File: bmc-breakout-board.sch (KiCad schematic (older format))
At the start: 42 parts, among them J1 PinHeader_2x4, J10 PinHeader_2x4, J11 PinHeader_2x05, J12 61300411121, J14 PCIE_BUS_x1, J15 0473460001, J16 PinHeader_1x07, J17 UE27AC54100, J2 PinHeader_2x13, J3 PinHeader_2x08, J4 61300411121, J5 ME1016813401101, J6 61300411121, J7 DC_SOCKET, J8 PinHeader_2x05, J9 PinHeader_1x07, Q1 BSS138AKA

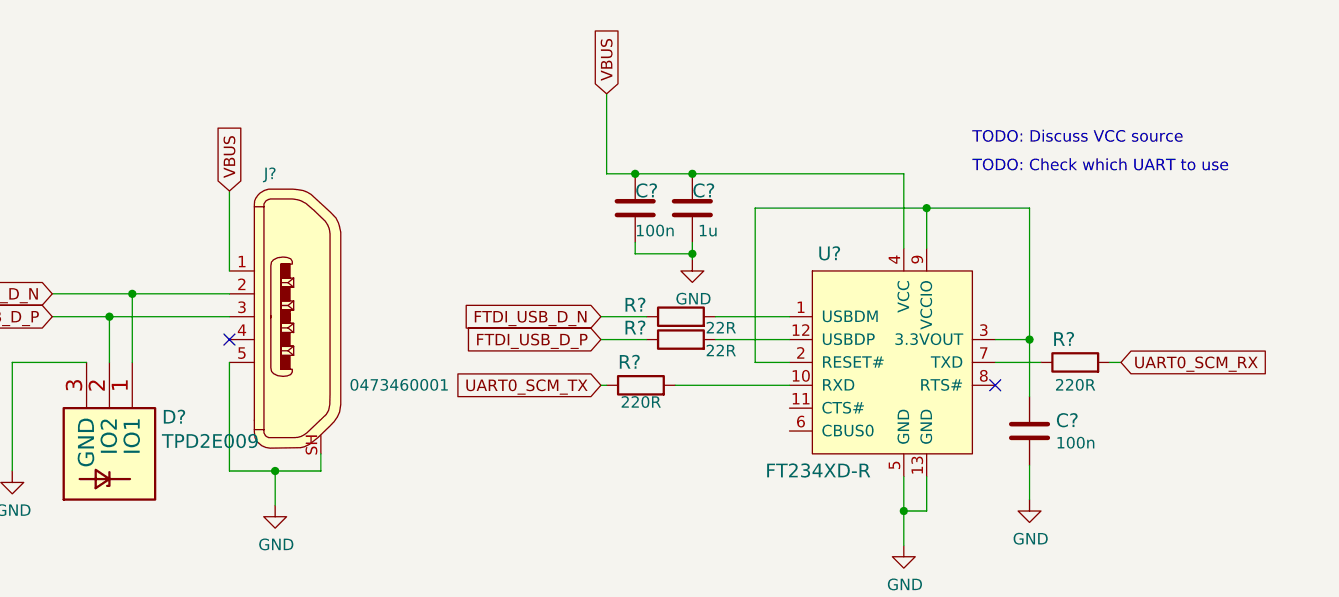
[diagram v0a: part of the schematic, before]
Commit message: Add FTDI circuit on PCB and do routing
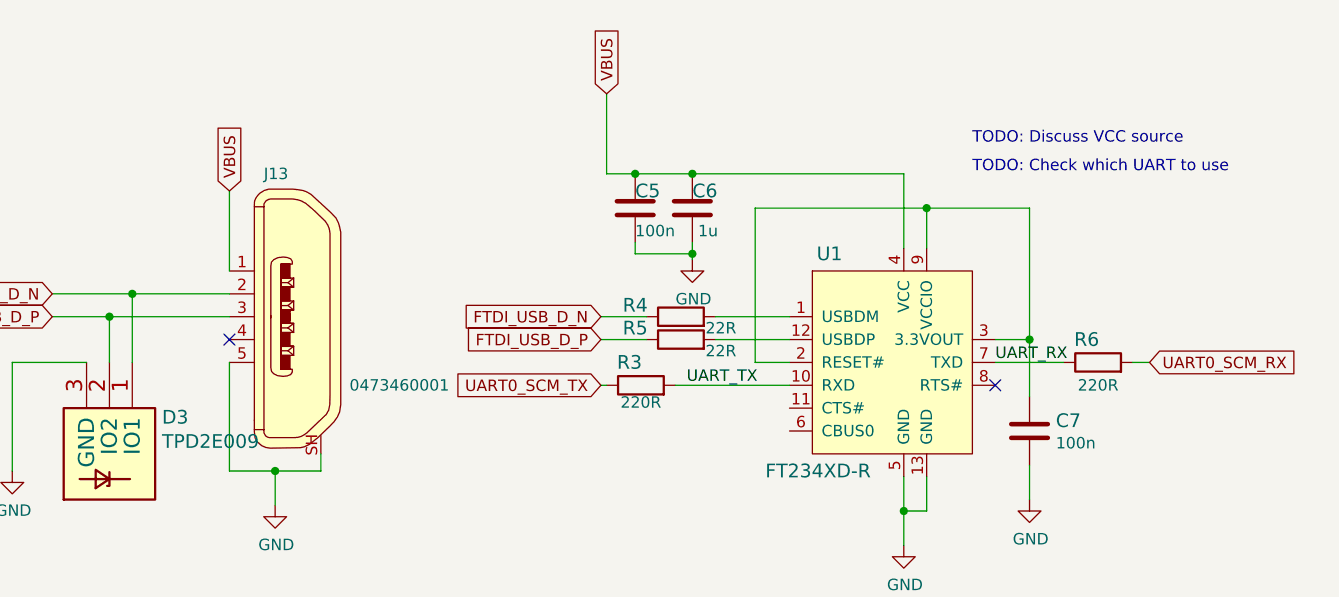
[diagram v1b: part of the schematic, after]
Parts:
- gave numbers to parts that had none: 10
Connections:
- net labels added: UART_RX, UART_TX
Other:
- moved on the sheet: R6
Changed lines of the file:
@@
 GND probes
 $Comp
-L bmc-breakout-board:FT234XD-R U?
+L bmc-breakout-board:FT234XD-R U1
 U 1 1 619D808C
 P 14225 6100
-F 0 "U?" H 14000 6475 60  0000 C CNN
+F 0 "U1" H 14000 6475 60  0000 C CNN
 F 1 "FT234XD-R" H 13950 5525 60  0000 C CNN
 F 2 "bmc-breakout-board-footprints:DFN-12-1EP_3x3mm" H 14425 6300 60  0001 L CNN
@@
 Connection ~ 14325 6850
 $Comp
-L bmc-breakout-board:GND #PWR?
+L bmc-breakout-board:GND #PWR0113
 U 1 1 61AF1FE7
 P 14325 7000
-F 0 "#PWR?" H 14325 6750 50  0001 C CNN
+F 0 "#PWR0113" H 14325 6750 50  0001 C CNN
 F 1 "GND" H 14330 6827 50  0000 C CNN
 F 2 "" H 14325 7000 50  0001 C CNN
@@
 	13000 6300 13025 6300
 Wire Wire Line
-	14725 6200 14925 6200
+	14725 6200 15025 6200
 Text GLabel 13000 6300 0    50   Input ~ 0
 UART0_SCM_TX
-Text GLabel 15275 6200 2    50   Input ~ 0
+Text GLabel 15400 6200 2    50   Input ~ 0
 UART0_SCM_RX
 $Comp
-L bmc-breakout-board:R_220R_0402 R?
+L bmc-breakout-board:R_220R_0402 R6
 U 1 1 61BE88F3
-P 15075 6200
-F 0 "R?" H 15025 6300 60  0000 C CNN
-F 1 "R_220R_0402" H 15075 6050 60  0001 C CNN
-F 2 "bmc-breakout-board-footprints:0402-res" H 15275 6400 60  0001 L CNN
-F 3 "" H 15075 6200 50  0001 C CNN
-F 4 "Panasonic" H 15275 6600 60  0001 L CNN "Manufacturer"
-F 5 "ERJ2GEJ221X" H 15275 6500 60  0001 L CNN "MPN"
-F 6 "220R" H 15075 6100 50  0000 C CNN "Val"
-	1    15075 6200
-	1    0    0    -1
-$EndComp
-$Comp
-L bmc-breakout-board:R_220R_0402 R?
+P 15175 6200
+F 0 "R6" H 15125 6300 60  0000 C CNN
+F 1 "R_220R_0402" H 15175 6050 60  0001 C CNN
+F 2 "bmc-breakout-board-footprints:0402-res" H 15375 6400 60  0001 L CNN
+F 3 "" H 15175 6200 50  0001 C CNN
+F 4 "Panasonic" H 15375 6600 60  0001 L CNN "Manufacturer"
+F 5 "ERJ2GEJ221X" H 15375 6500 60  0001 L CNN "MPN"
+F 6 "220R" H 15175 6100 50  0000 C CNN "Val"
+	1    15175 6200
+	1    0    0    -1
+$EndComp
+$Comp
+L bmc-breakout-board:R_220R_0402 R3
 U 1 1 61BE8BB6
 P 13175 6300
-F 0 "R?" H 13125 6400 60  0000 C CNN
+F 0 "R3" H 13125 6400 60  0000 C CNN
 F 1 "R_220R_0402" H 13175 6150 60  0001 C CNN
 F 2 "bmc-breakout-board-footprints:0402-res" H 13375 6500 60  0001 L CNN
@@
 	13325 6300 13825 6300
 Wire Wire Line
-	15225 6200 15275 6200
-$Comp
-L bmc-breakout-board:C_100n_0402 C?
+	15325 6200 15400 6200
+$Comp
+L bmc-breakout-board:C_100n_0402 C7
 U 1 1 61C08691
 P 14875 6500
-F 0 "C?" H 14760 6455 60  0000 R CNN
+F 0 "C7" H 14760 6455 60  0000 R CNN
 F 1 "C_100n_0402" H 14875 6350 60  0001 C CNN
 F 2 "bmc-breakout-board-footprints:0402-cap" H 15075 6700 60  0001 L CNN
@@
 	14875 6650 14875 6800
 $Comp
-L bmc-breakout-board:GND #PWR?
+L bmc-breakout-board:GND #PWR0114
 U 1 1 61C4C68C
 P 14875 6800
-F 0 "#PWR?" H 14875 6550 50  0001 C CNN
+F 0 "#PWR0114" H 14875 6550 50  0001 C CNN
 F 1 "GND" H 14880 6627 50  0000 C CNN
 F 2 "" H 14875 6800 50  0001 C CNN
@@
 	13025 5375 13150 5375
 $Comp
-L bmc-breakout-board:C_100n_0402 C?
+L bmc-breakout-board:C_100n_0402 C5
 U 1 1 61D03EE4
 P 13150 5525
-F 0 "C?" H 13150 5450 60  0000 R CNN
+F 0 "C5" H 13150 5450 60  0000 R CNN
 F 1 "C_100n_0402" H 13150 5375 60  0001 C CNN
 F 2 "bmc-breakout-board-footprints:0402-cap" H 13350 5725 60  0001 L CNN
@@
 	13150 5375 13400 5375
 $Comp
-L bmc-breakout-board:C_1u_0402 C?
+L bmc-breakout-board:C_1u_0402 C6
 U 1 1 61D40FF8
 P 13400 5525
-F 0 "C?" H 13400 5600 60  0000 L CNN
+F 0 "C6" H 13400 5600 60  0000 L CNN
 F 1 "C_1u_0402" H 13400 5375 60  0001 C CNN
 F 2 "bmc-breakout-board-footprints:0402-cap" H 13600 5725 60  0001 L CNN
@@
 Connection ~ 13400 5725
 $Comp
-L bmc-breakout-board:GND #PWR?
+L bmc-breakout-board:GND #PWR0115
 U 1 1 61D45FD6
 P 13400 5750
-F 0 "#PWR?" H 13400 5500 50  0001 C CNN
+F 0 "#PWR0115" H 13400 5500 50  0001 C CNN
 F 1 "GND" H 13405 5577 50  0000 C CNN
 F 2 "" H 13400 5750 50  0001 C CNN
@@
 $EndComp
 $Comp
-L bmc-breakout-board:R_22R_0402 R?
+L bmc-breakout-board:R_22R_0402 R5
 U 1 1 61DDB24D
 P 13350 6100
-F 0 "R?" H 13150 6150 60  0000 C CNN
+F 0 "R5" H 13150 6150 60  0000 C CNN
 F 1 "R_22R_0402" H 13350 5950 60  0001 C CNN
 F 2 "bmc-breakout-board-footprints:0402-res" H 13550 6300 60  0001 L CNN
@@
 $EndComp
 $Comp
-L bmc-breakout-board:R_22R_0402 R?
+L bmc-breakout-board:R_22R_0402 R4
 U 1 1 61E3AA54
 P 13350 6000
-F 0 "R?" H 13150 6050 60  0000 C CNN
+F 0 "R4" H 13150 6050 60  0000 C CNN
 F 1 "R_22R_0402" H 13350 5850 60  0001 C CNN
 F 2 "bmc-breakout-board-footprints:0402-res" H 13550 6200 60  0001 L CNN
@@
 VBUS
 $Comp
-L bmc-breakout-board:TPD2E009 D?
+L bmc-breakout-board:TPD2E009 D3
 U 1 1 61F54A7F
 P 10950 6400
-F 0 "D?" V 10990 6530 60  0000 L CNN
+F 0 "D3" V 10990 6530 60  0000 L CNN
 F 1 "TPD2E009" V 11096 6530 60  0000 L CNN
 F 2 "bmc-breakout-board-footprints:SOT-3" H 11000 6600 60  0001 C CNN
@@
 	10425 6200 10425 6675
 $Comp
-L bmc-breakout-board:GND #PWR?
+L bmc-breakout-board:GND #PWR0116
 U 1 1 61F54A8D
 P 10425 6675
-F 0 "#PWR?" H 10425 6425 50  0001 C CNN
+F 0 "#PWR0116" H 10425 6425 50  0001 C CNN
 F 1 "GND" H 10430 6502 50  0000 C CNN
 F 2 "" H 10425 6675 50  0001 C CNN
@@
 	11375 6675 11575 6675
 $Comp
-L bmc-breakout-board:GND #PWR?
+L bmc-breakout-board:GND #PWR0117
 U 1 1 61F54A94
 P 11575 6825
-F 0 "#PWR?" H 11575 6575 50  0001 C CNN
+F 0 "#PWR0117" H 11575 6575 50  0001 C CNN
 F 1 "GND" H 11580 6652 50  0000 C CNN
 F 2 "" H 11575 6825 50  0001 C CNN
@@
 NoConn ~ 11375 6100
 $Comp
-L bmc-breakout-board:0473460001 J?
+L bmc-breakout-board:0473460001 J13
 U 1 1 61F54AA2
 P 11675 6000
-F 0 "J?" H 11825 6625 50  0000 R CNN
+F 0 "J13" H 11825 6625 50  0000 R CNN
 F 1 "0473460001" H 11450 5700 50  0000 R CNN
 F 2 "bmc-breakout-board-footprints:USB_Micro_B_Female_0473460001" H 11875 6200 60  0001 L CNN
@@
 Text GLabel 10600 5900 0    50   Input ~ 0
 FTDI_USB_D_N
+Text Label 13375 6300 0    50   ~ 0
+UART_TX
+Text Label 14725 6200 0    50   ~ 0
+UART_RX
 $EndSCHEMATC

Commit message: Add power filtering
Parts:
- added C? (x2): C_100n_0402_16V, antmicro-footprints:0402-cap, symbol antmicroCapacitorsmisc:C_100n_0402_16V
- added C?: C_3u3_1206_100V, antmicro-footprints:1206-cap, symbol antmicroCapacitorsmisc:C_3u3_1206_100V
- added L?: 744235900, antmicro-footprints:744235900, symbol antmicroFixedInductors:744235900
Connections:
- net labels added: P12V_AUX_IN
- wire segments 340 -> 359
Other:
- note added: "Power filtering"
- moved on the sheet: J14, R1, R2

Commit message: Update filtering circuit
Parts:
- removed C?: C_3u3_1206_100V, antmicro-footprints:1206-cap, symbol antmicroCapacitorsmisc:C_3u3_1206_100V
- added C?: C_10u_25V_0603, bmc-breakout-board-footprints:0603-cap, symbol bmc-breakout-board:C_10u_25V_0603
- added C? (x2): C_1n_0603, bmc-breakout-board-footprints:0603-cap, symbol bmc-breakout-board:C_1n_0603
- C? (x2): footprint antmicro-footprints:0402-cap -> bmc-breakout-board-footprints:0402-cap; symbol antmicroCapacitorsmisc:C_100n_0402_16V -> bmc-breakout-board:C_100n_0402_16V
- L?: footprint antmicro-footprints:744235900 -> bmc-breakout-board-footprints:744235900; symbol antmicroFixedInductors:744235900 -> bmc-breakout-board:744235900
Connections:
- net labels added: GND_IN
- wire segments 359 -> 368
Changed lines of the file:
@@
 Wire Wire Line
 	14450 3125 14450 3525
-$Comp
-L bmc-breakout-board:GND #PWR0110
-U 1 1 60D4DCD1
-P 14450 3675
-F 0 "#PWR0110" H 14450 3425 50  0001 C CNN
-F 1 "GND" H 14455 3502 50  0000 C CNN
-F 2 "" H 14450 3675 50  0001 C CNN
-F 3 "" H 14450 3675 50  0001 C CNN
-	1    14450 3675
-	1    0    0    -1
-$EndComp
 Wire Wire Line
 	14450 3125 14575 3125
@@
 	14450 3525 14575 3525
 Connection ~ 14450 3525
-Wire Wire Line
-	14450 3525 14450 3675
 Wire Wire Line
 	14575 3325 14325 3325
@@
 UART_RX
 $Comp
-L antmicroCapacitorsmisc:C_100n_0402_16V C?
+L bmc-breakout-board:C_100n_0402_16V C?
 U 1 1 6211016B
 P 13450 4300
 F 0 "C?" H 13565 4345 60  0000 L CNN
 F 1 "C_100n_0402_16V" H 13450 4150 60  0001 C CNN
-F 2 "antmicro-footprints:0402-cap" H 13650 4500 60  0001 L CNN
+F 2 "bmc-breakout-board-footprints:0402-cap" H 13650 4500 60  0001 L CNN
 F 3 "" H 13450 4300 50  0001 C CNN
 F 4 "MULTICOMP" H 13650 4700 60  0001 L CNN "Manufacturer"
@@
 $EndComp
 $Comp
-L antmicroCapacitorsmisc:C_3u3_1206_100V C?
-U 1 1 62116EE7
-P 14925 4300
-F 0 "C?" H 14925 4400 60  0000 L CNN
-F 1 "C_3u3_1206_100V" H 14925 4150 60  0001 C CNN
-F 2 "antmicro-footprints:1206-cap" H 15125 4500 60  0001 L CNN
-F 3 "" H 14925 4300 50  0001 C CNN
-F 4 "TDK" H 15125 4700 60  0001 L CNN "Manufacturer"
-F 5 "C3216X7S2A335K160AB" H 15125 4600 60  0001 L CNN "MPN"
-F 6 "3.3u" H 14925 4200 50  0000 L CNN "Val"
-	1    14925 4300
-	1    0    0    -1
-$EndComp
-$Comp
-L antmicroFixedInductors:744235900 L?
+L bmc-breakout-board:744235900 L?
 U 1 1 621486C2
 P 14050 4300
 F 0 "L?" H 14050 4581 50  0000 C CNN
 F 1 "744235900" H 14050 4490 50  0000 C CNN
-F 2 "antmicro-footprints:744235900" H 14050 4300 50  0001 C CNN
+F 2 "bmc-breakout-board-footprints:744235900" H 14050 4300 50  0001 C CNN
 F 3 "~" H 14050 4300 50  0001 C CNN
 F 4 "Wurth Elektronik" H 14050 4300 50  0001 C CNN "Manufacturer"
@@
 $EndComp
 $Comp
-L antmicroCapacitorsmisc:C_100n_0402_16V C?
+L bmc-breakout-board:C_100n_0402_16V C?
 U 1 1 621BA923
-P 14575 4300
-F 0 "C?" H 14600 4400 60  0000 L CNN
-F 1 "C_100n_0402_16V" H 14575 4150 60  0001 C CNN
-F 2 "antmicro-footprints:0402-cap" H 14775 4500 60  0001 L CNN
-F 3 "" H 14575 4300 50  0001 C CNN
-F 4 "MULTICOMP" H 14775 4700 60  0001 L CNN "Manufacturer"
-F 5 "MC0402B104K160CT" H 14775 4600 60  0001 L CNN "MPN"
-F 6 "100n" H 14600 4200 50  0000 L CNN "Val"
-	1    14575 4300
+P 14925 4300
+F 0 "C?" H 14950 4400 60  0000 L CNN
+F 1 "C_100n_0402_16V" H 14925 4150 60  0001 C CNN
+F 2 "bmc-breakout-board-footprints:0402-cap" H 15125 4500 60  0001 L CNN
+F 3 "" H 14925 4300 50  0001 C CNN
+F 4 "MULTICOMP" H 15125 4700 60  0001 L CNN "Manufacturer"
+F 5 "MC0402B104K160CT" H 15125 4600 60  0001 L CNN "MPN"
+F 6 "100n" H 14950 4200 50  0000 L CNN "Val"
+	1    14925 4300
 	1    0    0    -1
 $EndComp
@@
 Wire Wire Line
 	14250 4575 14575 4575
-Wire Wire Line
-	14925 4575 14925 4450
 Wire Wire Line
 	14575 4450 14575 4575
@@
 Wire Wire Line
 	13450 4450 13450 4575
-Connection ~ 14925 4575
-Wire Wire Line
-	15475 4025 14925 4025
-Wire Wire Line
-	12900 4050 13450 4050
+Wire Wire Line
+	15475 4025 15250 4025
+Wire Wire Line
+	12900 4050 13175 4050
 Text GLabel 15475 4025 2    50   Input ~ 0
 P12V_AUX
 Connection ~ 13450 4050
 Connection ~ 14925 4025
-$Comp
-L bmc-breakout-board:GND #PWR0109
-U 1 1 60323931
-P 14625 1550
-F 0 "#PWR0109" H 14625 1300 50  0001 C CNN
-F 1 "GND" H 14630 1377 50  0000 C CNN
-F 2 "" H 14625 1550 50  0001 C CNN
-F 3 "" H 14625 1550 50  0001 C CNN
-	1    14625 1550
-	1    0    0    -1
-$EndComp
 Wire Wire Line
 	14625 1375 14625 1550
@@
 $EndComp
 Wire Wire Line
-	14925 4575 14925 4775
+	15250 4575 15250 4775
 $Comp
 L bmc-breakout-board:GND #PWR?
 U 1 1 622D6B0C
-P 14925 4775
-F 0 "#PWR?" H 14925 4525 50  0001 C CNN
-F 1 "GND" H 14930 4602 50  0000 C CNN
-F 2 "" H 14925 4775 50  0001 C CNN
-F 3 "" H 14925 4775 50  0001 C CNN
-	1    14925 4775
+P 15250 4775
+F 0 "#PWR?" H 15250 4525 50  0001 C CNN
+F 1 "GND" H 15255 4602 50  0000 C CNN
+F 2 "" H 15250 4775 50  0001 C CNN
+F 3 "" H 15250 4775 50  0001 C CNN
+	1    15250 4775
 	1    0    0    -1
 $EndComp
@@
 Text GLabel 12900 4050 0    50   Input ~ 0
 P12V_AUX_IN
-Text Notes 13375 3850 0    79   ~ 0
+Text Notes 13675 3875 0    79   ~ 0
 Power filtering
+Text GLabel 14625 1550 0    50   Input ~ 0
+GND_IN
+Text GLabel 12875 4575 0    50   Input ~ 0
+GND_IN
+Wire Wire Line
+	12875 4575 13175 4575
+Connection ~ 13450 4575
+$Comp
+L bmc-breakout-board:C_10u_25V_0603 C?
+U 1 1 60C84DD9
+P 14575 4300
+F 0 "C?" H 14575 4400 60  0000 L CNN
+F 1 "C_10u_25V_0603" H 14575 4150 60  0001 C CNN
+F 2 "bmc-breakout-board-footprints:0603-cap" H 14775 4500 60  0001 L CNN
+F 3 "" H 14575 4300 50  0001 C CNN
+F 4 "TDK" H 14775 4700 60  0001 L CNN "Manufacturer"
+F 5 "C1608X5R1E106M080AC" H 14775 4600 60  0001 L CNN "MPN"
+F 6 "10u/25V" H 14575 4175 50  0000 L CNN "Val"
+	1    14575 4300
+	1    0    0    -1
+$EndComp
+$Comp
+L bmc-breakout-board:C_1n_0603 C?
+U 1 1 60CA6672
+P 15250 4300
+F 0 "C?" H 15275 4400 60  0000 L CNN
+F 1 "C_1n_0603" H 15250 4150 60  0001 C CNN
+F 2 "bmc-breakout-board-footprints:0603-cap" H 15450 4500 60  0001 L CNN
+F 3 "" H 15250 4300 50  0001 C CNN
+F 4 "AVX" H 15450 4700 60  0001 L CNN "Manufacturer"
+F 5 "06031C102JAT2A" H 15450 4600 60  0001 L CNN "MPN"
+F 6 "1n" H 15250 4200 50  0000 L CNN "Val"
+	1    15250 4300
+	1    0    0    -1
+$EndComp
+Wire Wire Line
+	15250 4150 15250 4025
+Connection ~ 15250 4025
+Wire Wire Line
+	15250 4025 14925 4025
+Wire Wire Line
+	14925 4450 14925 4575
+Connection ~ 14925 4575
+Wire Wire Line
+	14925 4575 15250 4575
+Wire Wire Line
+	15250 4450 15250 4575
+Connection ~ 15250 4575
+Text GLabel 14200 3525 0    50   Input ~ 0
+GND_IN
+Wire Wire Line
+	14200 3525 14450 3525
+$Comp
+L bmc-breakout-board:C_1n_0603 C?
+U 1 1 60DFCD01
+P 13175 4300
+F 0 "C?" H 13200 4400 60  0000 L CNN
+F 1 "C_1n_0603" H 13175 4150 60  0001 C CNN
+F 2 "bmc-breakout-board-footprints:0603-cap" H 13375 4500 60  0001 L CNN
+F 3 "" H 13175 4300 50  0001 C CNN
+F 4 "AVX" H 13375 4700 60  0001 L CNN "Manufacturer"
+F 5 "06031C102JAT2A" H 13375 4600 60  0001 L CNN "MPN"
+F 6 "1n" H 13175 4200 50  0000 L CNN "Val"
+	1    13175 4300
+	1    0    0    -1
+$EndComp
+Wire Wire Line
+	13175 4150 13175 4050
+Connection ~ 13175 4050
+Wire Wire Line
+	13175 4050 13450 4050
+Wire Wire Line
+	13175 4450 13175 4575
+Connection ~ 13175 4575
+Wire Wire Line
+	13175 4575 13450 4575
 $EndSCHEMATC

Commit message: Change power switch
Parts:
- removed Q1: BSS138AKA, bmc-breakout-board-footprints:SOT-23-3, symbol bmc-breakout-board:BSS138AKA
- removed S1: JS202011SCQN, bmc-breakout-board-footprints:Switch_Slide_JS202011SCQN, symbol bmc-breakout-board:JS202011SCQN
- added N2: oshw_logo, antmicro-footprints:oshw-logo, symbol antmicroMechanicalParts:oshw_logo
- added Q?: SI2337DS, antmicro-footprints:SOT-23-3, symbol antmicroTransistorsFETsMOSFETsSingle:SI2337DS
- added S?: EG1218, antmicro-footprints:Switch_Slide_11.6x4mm_EG1218, symbol antmicroSlideSwitches:EG1218
- gave numbers to parts that had none: 6
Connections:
- wire segments 368 -> 359
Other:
- note removed: "TODO: Check which UART to use"
- note removed: "TODO: Discuss VCC source"
- moved on the sheet: C10, C11, C12, C5, C6, C7, C8, C9, D1, D2, D3, J13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
